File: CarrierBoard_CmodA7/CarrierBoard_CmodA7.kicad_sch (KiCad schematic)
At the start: 48 parts

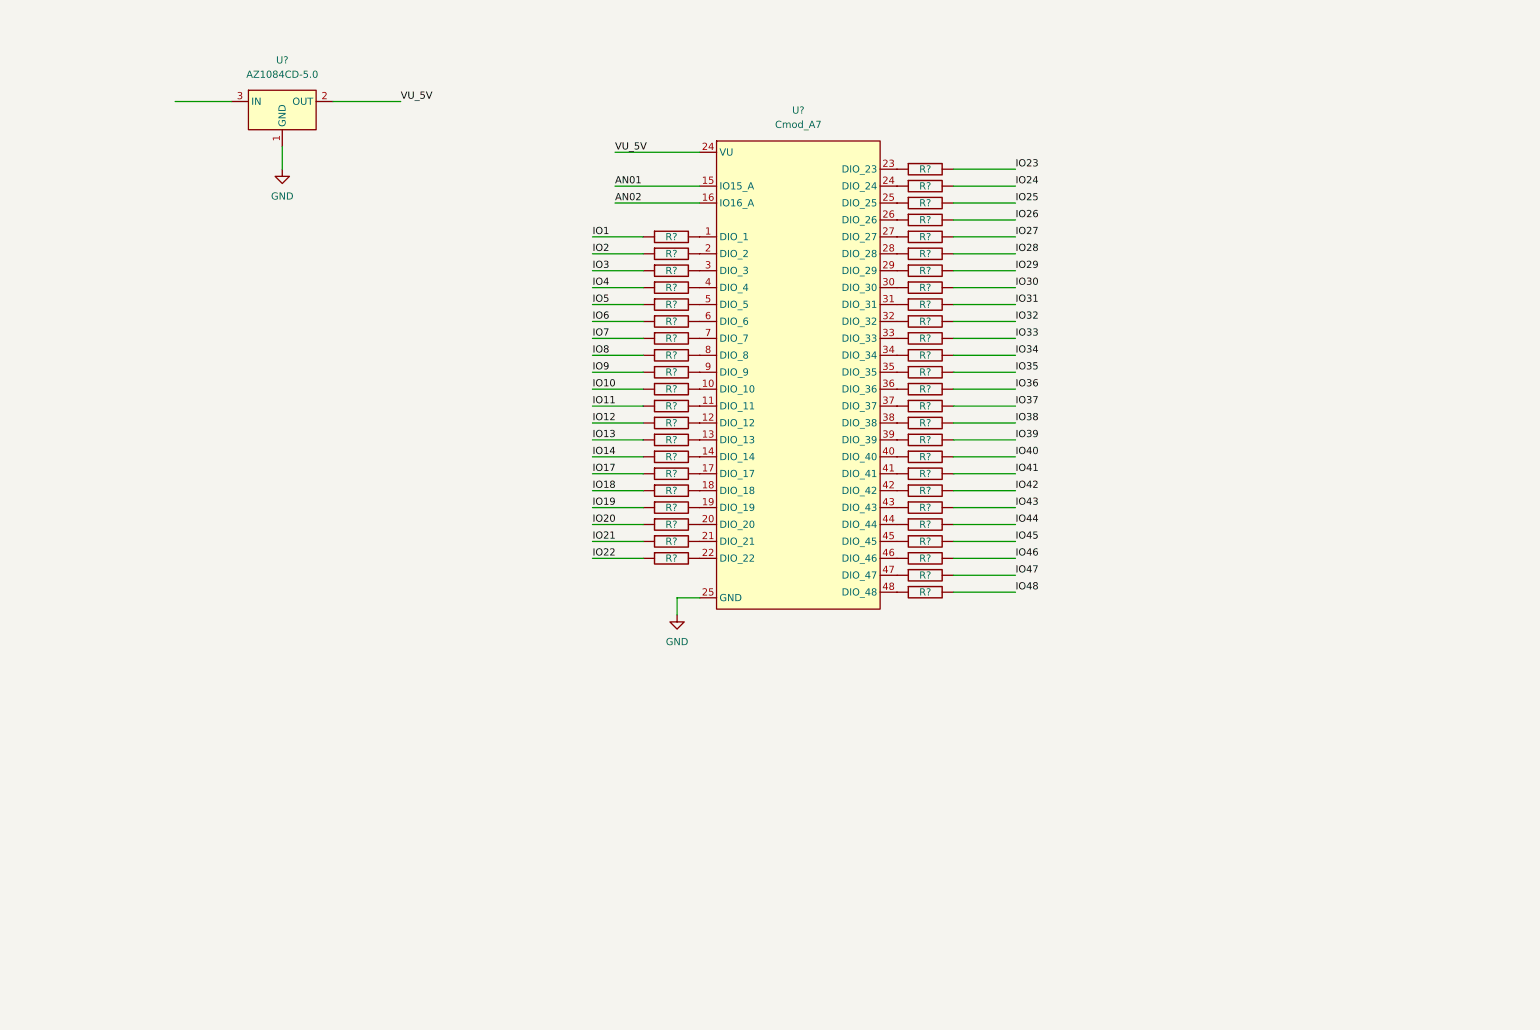
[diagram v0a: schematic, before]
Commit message: Añadidos conectores PMOD
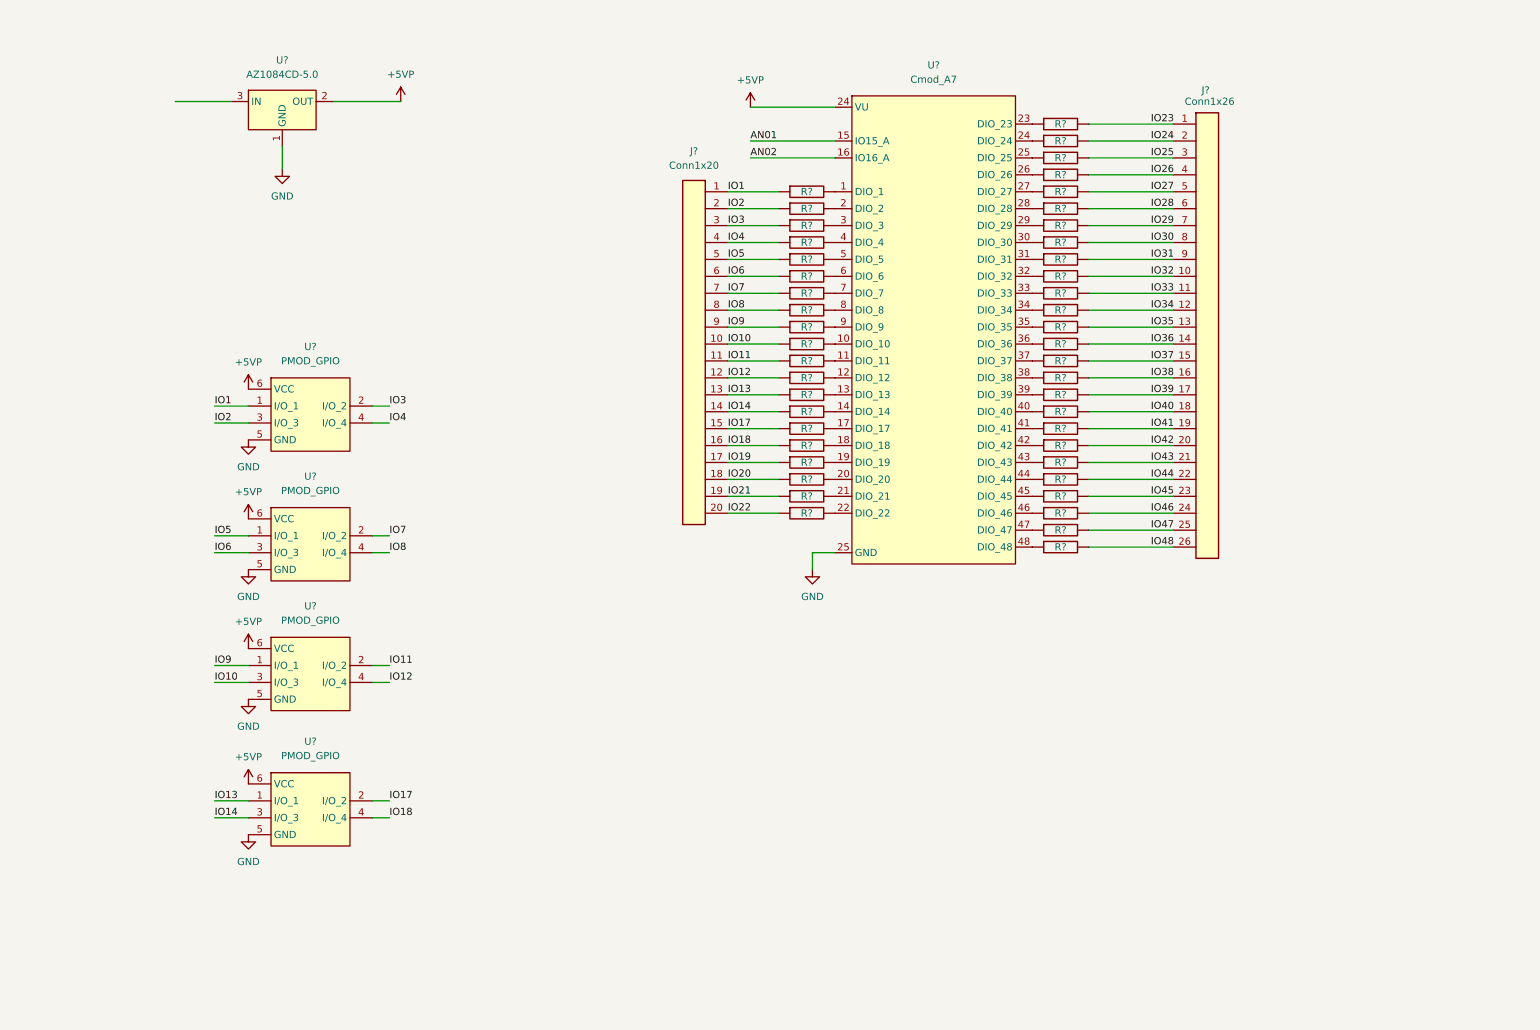
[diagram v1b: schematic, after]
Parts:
- added J?: Conn1x20, Connector_PinHeader_2.54mm:PinHeader_1x20_P2.54mm_Vertical, symbol Herranz - Gen Connectors:Conn1x20
- added J?: Conn1x26, Connector_PinHeader_2.54mm:PinHeader_1x26_P2.54mm_Vertical, symbol Herranz - Gen Connectors:Conn1x26
- added U? (x4): PMOD_GPIO, Connector_PinHeader_2.54mm:PinHeader_2x03_P2.54mm_Horizontal, symbol Herranz - Various:PMOD_GPIO
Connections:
- net GND: now also U?.5 (GND), U?.5 (GND), U?.5 (GND), U?.5 (GND)
- net IO1: now also J?.1 (Pin_1), U?.1 (I/O_1)
- net IO10: now also J?.10 (Pin_10), U?.3 (I/O_3)
- net IO11: now also J?.11 (Pin_11), U?.2 (I/O_2)
- net IO12: now also J?.12 (Pin_12), U?.4 (I/O_4)
- net IO13: now also J?.13 (Pin_13), U?.1 (I/O_1)
- net IO14: now also J?.14 (Pin_14), U?.3 (I/O_3)
- net IO17: now also J?.15 (Pin_15), U?.2 (I/O_2)
- net IO18: now also J?.16 (Pin_16), U?.4 (I/O_4)
- net IO19: now also J?.17 (Pin_17)
- net IO2: now also J?.2 (Pin_2), U?.3 (I/O_3)
- net IO20: now also J?.18 (Pin_18)
- net IO21: now also J?.19 (Pin_19)
- net IO22: now also J?.20 (Pin_20)
- net IO23: now also J?.1 (Pin_1)
- net IO24: now also J?.2 (Pin_2)
- net IO25: now also J?.3 (Pin_3)
- net IO26: now also J?.4 (Pin_4)
- net IO27: now also J?.5 (Pin_5)
- net IO28: now also J?.6 (Pin_6)
- net IO29: now also J?.7 (Pin_7)
- net IO3: now also J?.3 (Pin_3), U?.2 (I/O_2)
- net IO30: now also J?.8 (Pin_8)
- net IO31: now also J?.9 (Pin_9)
- net IO32: now also J?.10 (Pin_10)
- net IO33: now also J?.11 (Pin_11)
- net IO34: now also J?.12 (Pin_12)
- net IO35: now also J?.13 (Pin_13)
- net IO36: now also J?.14 (Pin_14)
- net IO37: now also J?.15 (Pin_15)
- net IO38: now also J?.16 (Pin_16)
- net IO39: now also J?.17 (Pin_17)
- net IO4: now also J?.4 (Pin_4), U?.4 (I/O_4)
- net IO40: now also J?.18 (Pin_18)
- net IO41: now also J?.19 (Pin_19)
- net IO42: now also J?.20 (Pin_20)
- net IO43: now also J?.21 (Pin_21)
- net IO44: now also J?.22 (Pin_22)
- net IO45: now also J?.23 (Pin_23)
- net IO46: now also J?.24 (Pin_24)
- net IO47: now also J?.25 (Pin_25)
- net IO48: now also J?.26 (Pin_26)
- net IO5: now also J?.5 (Pin_5), U?.1 (I/O_1)
- net IO6: now also J?.6 (Pin_6), U?.3 (I/O_3)
- net IO7: now also J?.7 (Pin_7), U?.2 (I/O_2)
- net IO8: now also J?.8 (Pin_8), U?.4 (I/O_4)
- net IO9: now also J?.9 (Pin_9), U?.1 (I/O_1)
- net VU_5V renamed +5VP
- net +5VP: now also U?.6 (VCC), U?.6 (VCC), U?.6 (VCC), U?.6 (VCC)
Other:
- moved on the sheet: R?, U?

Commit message: añadido red ADC
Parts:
- added R?: 140_P, Resistor_SMD:R_0603_1608Metric, symbol Herranz - Resistors (0603):140_P
- added R?: 845_P, Resistor_SMD:R_0603_1608Metric, symbol Herranz - Resistors (0603):845_P
- added R?: 1.0K_P, Resistor_SMD:R_0603_1608Metric, symbol Herranz - Resistors (0603):1.0K_P
- added R?: 2.32K_P, Resistor_SMD:R_0603_1608Metric, symbol Herranz - Resistors (0603):2.32K_P
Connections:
- net GND: now also R?.1, R?.2
- new net: R?.1, R?.2, R?.2
- new net GNDA: R?.1
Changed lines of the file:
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@@
 (kicad_sch (version 20211123) (generator eeschema)
   (paper "A4")
+  (junction (at 161 136) (diameter 0) (color 0 0 0 0)
+  )
+  (junction (at 134 151) (diameter 0) (color 0 0 0 0)
+  )
+  (junction (at 161 151) (diameter 0) (color 0 0 0 0)
+  )
   (wire (pts (xy 141 35) (xy 156 35))
     (stroke (width 0) (type default) (color 0 0 0 0))
@@
     (stroke (width 0) (type default) (color 0 0 0 0))
   )
+  (wire (pts (xy 152 136) (xy 161 136))
+    (stroke (width 0) (type default) (color 0 0 0 0))
+  )
   (wire (pts (xy 201 38) (xy 216 38))
     (stroke (width 0) (type default) (color 0 0 0 0))
@@
     (stroke (width 0) (type default) (color 0 0 0 0))
   )
+  (wire (pts (xy 128 136) (xy 142 136))
+    (stroke (width 0) (type default) (color 0 0 0 0))
+  )
   (wire (pts (xy 201 101) (xy 216 101))
     (stroke (width 0) (type default) (color 0 0 0 0))
   )
+  (wire (pts (xy 161 136) (xy 161 134))
+    (stroke (width 0) (type default) (color 0 0 0 0))
+  )
   (wire (pts (xy 201 95) (xy 216 95))
     (stroke (width 0) (type default) (color 0 0 0 0))
@@
     (stroke (width 0) (type default) (color 0 0 0 0))
   )
+  (wire (pts (xy 134 151) (xy 134 154))
+    (stroke (width 0) (type default) (color 0 0 0 0))
+  )
   (wire (pts (xy 46 134) (xy 52 134))
     (stroke (width 0) (type default) (color 0 0 0 0))
@@
     (stroke (width 0) (type default) (color 0 0 0 0))
   )
+  (wire (pts (xy 152 151) (xy 161 151))
+    (stroke (width 0) (type default) (color 0 0 0 0))
+  )
   (wire (pts (xy 74 88) (xy 77 88))
     (stroke (width 0) (type default) (color 0 0 0 0))
@@
     (stroke (width 0) (type default) (color 0 0 0 0))
   )
+  (wire (pts (xy 161 136) (xy 161 138))
+    (stroke (width 0) (type default) (color 0 0 0 0))
+  )
   (wire (pts (xy 137 107) (xy 146 107))
     (stroke (width 0) (type default) (color 0 0 0 0))
   )
+  (wire (pts (xy 161 154) (xy 161 151))
+    (stroke (width 0) (type default) (color 0 0 0 0))
+  )
   (wire (pts (xy 201 92) (xy 216 92))
     (stroke (width 0) (type default) (color 0 0 0 0))
@@
     (stroke (width 0) (type default) (color 0 0 0 0))
   )
+  (wire (pts (xy 128 151) (xy 134 151))
+    (stroke (width 0) (type default) (color 0 0 0 0))
+  )
   (wire (pts (xy 137 104) (xy 146 104))
     (stroke (width 0) (type default) (color 0 0 0 0))
@@
     (stroke (width 0) (type default) (color 0 0 0 0))
   )
+  (wire (pts (xy 134 151) (xy 142 151))
+    (stroke (width 0) (type default) (color 0 0 0 0))
+  )
   (wire (pts (xy 137 74) (xy 146 74))
     (stroke (width 0) (type default) (color 0 0 0 0))
@@
   )
   (wire (pts (xy 201 65) (xy 216 65))
+    (stroke (width 0) (type default) (color 0 0 0 0))
+  )
+  (wire (pts (xy 161 151) (xy 161 148))
     (stroke (width 0) (type default) (color 0 0 0 0))
   )
@@
     )
     (pin "1")
+  )
+  (symbol (lib_id "Herranz - Resistors (0603):140_P") (at 147 135 0) (unit 1)
+    (in_bom yes) (on_board yes) (fields_autoplaced)
+    (property "Reference" "R?" (id 0) (at 147 127 0))
+    (property "Value" "140_P" (id 1) (at 147 129.54 0))
+    (property "Footprint" "Resistor_SMD:R_0603_1608Metric" (id 2) (at 147 132 0)
+      (effects (font (size 1.27 1.27)) hide)
+    )
+    (property "Datasheet" "" (id 3) (at 147 135 0)
+      (effects (font (size 1.27 1.27)) hide)
+    )
+    (property "Size" "0603" (id 4) (at 147 132.08 0))
+    (property "Precision" "X" (id 5) (at 147 135 0)
+      (effects (font (size 1.27 1.27)) hide)
+    )
+    (property "PartNum1" "RN73H1JTTD1400F50 " (id 6) (at 147 135 0)
+      (effects (font (size 1.27 1.27)) hide)
+    )
+    (property "Mnf1" "KOA Speer" (id 7) (at 147 135 0)
+      (effects (font (size 1.27 1.27)) hide)
+    )
+    (pin "1")
+    (pin "2")
   )
   (symbol (lib_id "Herranz - Resistors (0603):1.0K") (at 196 49 0) (unit 1)
@@
     (pin "2")
   )
+  (symbol (lib_id "Herranz - Resistors (0603):845_P") (at 147 150 0) (unit 1)
+    (in_bom yes) (on_board yes) (fields_autoplaced)
+    (property "Reference" "R?" (id 0) (at 147 142.43 0))
+    (property "Value" "845_P" (id 1) (at 147 144.97 0))
+    (property "Footprint" "Resistor_SMD:R_0603_1608Metric" (id 2) (at 147 147 0)
+      (effects (font (size 1.27 1.27)) hide)
+    )
+    (property "Datasheet" "" (id 3) (at 147 150 0)
+      (effects (font (size 1.27 1.27)) hide)
+    )
+    (property "Size" "0603" (id 4) (at 147 147.51 0))
+    (pin "1")
+    (pin "2")
+  )
   (symbol (lib_id "Herranz - Resistors (0603):1.0K") (at 196 94 0) (unit 1)
     (in_bom yes) (on_board yes)
@@
     (pin "2")
   )
+  (symbol (lib_id "power:GNDA") (at 134 154 0) (unit 1)
+    (in_bom yes) (on_board yes) (fields_autoplaced)
+    (property "Reference" "#PWR?" (id 0) (at 134 160.35 0)
+      (effects (font (size 1.27 1.27)) hide)
+    )
+    (property "Value" "GNDA" (id 1) (at 134 159.21 0))
+    (property "Footprint" "" (id 2) (at 134 154 0)
+      (effects (font (size 1.27 1.27)) hide)
+    )
+    (property "Datasheet" "" (id 3) (at 134 154 0)
+      (effects (font (size 1.27 1.27)) hide)
+    )
+    (pin "1")
+  )
   (symbol (lib_id "Herranz - Resistors (0603):1.0K") (at 196 109 0) (unit 1)
     (in_bom yes) (on_board yes)
@@
     (pin "2")
   )
+  (symbol (lib_id "power:GND") (at 161 154 0) (unit 1)
+    (in_bom yes) (on_board yes) (fields_autoplaced)
+    (property "Reference" "#PWR?" (id 0) (at 161 160.35 0)
+      (effects (font (size 1.27 1.27)) hide)
+    )
+    (property "Value" "GND" (id 1) (at 161 158.8 0))
+    (property "Footprint" "" (id 2) (at 161 154 0)
+      (effects (font (size 1.27 1.27)) hide)
+    )
+    (property "Datasheet" "" (id 3) (at 161 154 0)
+      (effects (font (size 1.27 1.27)) hide)
+    )
+    (pin "1")
+  )
   (symbol (lib_id "Herranz - Resistors (0603):1.0K") (at 196 67 0) (unit 1)
     (in_bom yes) (on_board yes)
@@
     (property "Size" "0603" (id 4) (at 196 55.61 0)
       (effects (font (size 1.27 1.27)) hide)
+    )
+    (pin "1")
+    (pin "2")
+  )
+  (symbol (lib_id "Herranz - Resistors (0603):1.0K_P") (at 160 143 90) (unit 1)
+    (in_bom yes) (on_board yes) (fields_autoplaced)
+    (property "Reference" "R?" (id 0) (at 163.83 140.4599 90)
+      (effects (font (size 1.27 1.27)) (justify right))
+    )
+    (property "Value" "1.0K_P" (id 1) (at 163.83 142.9999 90)
+      (effects (font (size 1.27 1.27)) (justify right))
+    )
+    (property "Footprint" "Resistor_SMD:R_0603_1608Metric" (id 2) (at 157 143 0)
+      (effects (font (size 1.27 1.27)) hide)
+    )
+    (property "Datasheet" "" (id 3) (at 160 143 0)
+      (effects (font (size 1.27 1.27)) hide)
+    )
+    (property "Size" "0603" (id 4) (at 163.83 145.5399 90)
+      (effects (font (size 1.27 1.27)) (justify right))
     )
     (pin "1")
@@
     (pin "2")
   )
+  (symbol (lib_id "Herranz - Resistors (0603):2.32K_P") (at 160 129 90) (unit 1)
+    (in_bom yes) (on_board yes) (fields_autoplaced)
+    (property "Reference" "R?" (id 0) (at 163.83 126.4599 90)
+      (effects (font (size 1.27 1.27)) (justify right))
+    )
+    (property "Value" "2.32K_P" (id 1) (at 163.83 128.9999 90)
+      (effects (font (size 1.27 1.27)) (justify right))
+    )
+    (property "Footprint" "Resistor_SMD:R_0603_1608Metric" (id 2) (at 157 129 0)
+      (effects (font (size 1.27 1.27)) hide)
+    )
+    (property "Datasheet" "" (id 3) (at 160 129 0)
+      (effects (font (size 1.27 1.27)) hide)
+    )
+    (property "Size" "0603" (id 4) (at 163.83 131.5399 90)
+      (effects (font (size 1.27 1.27)) (justify right))
+    )
+    (pin "1")
+    (pin "2")
+  )
   (symbol (lib_id "Herranz - Resistors (0603):1.0K") (at 196 85 0) (unit 1)
     (in_bom yes) (on_board yes)
@@
       (reference "#PWR?") (unit 1) (value "GND") (footprint "")
     )
+    (path "/bcaf2dca-bfb6-45b7-bff9-b0d7d064715a"
+      (reference "#PWR?") (unit 1) (value "GNDA") (footprint "")
+    )
+    (path "/beb53e2f-63cb-4982-a0e9-8eccccd29909"
+      (reference "#PWR?") (unit 1) (value "GND") (footprint "")
+    )
     (path "/e23fe0f2-2b10-4e4e-a248-1590767a0e0e"
       (reference "#PWR?") (unit 1) (value "GND") (footprint "")
@@
       (reference "R?") (unit 1) (value "1.0K") (footprint "Resistor_SMD:R_0603_1608Metric")
     )
+    (path "/4b68fabc-0578-4223-a045-7ebbc31dc0d9"
+      (reference "R?") (unit 1) (value "140_P") (footprint "Resistor_SMD:R_0603_1608Metric")
+    )
     (path "/4c0f8c6c-ed32-407d-8144-2572e6613b1a"
       (reference "R?") (unit 1) (value "1.0K") (footprint "Resistor_SMD:R_0603_1608Metric")
@@
       (reference "R?") (unit 1) (value "1.0K") (footprint "Resistor_SMD:R_0603_1608Metric")
     )
+    (path "/62dc1d02-190f-4c9d-8ded-2c7f4b299c50"
+      (reference "R?") (unit 1) (value "845_P") (footprint "Resistor_SMD:R_0603_1608Metric")
+    )
     (path "/682ef0b5-4757-486e-bfa0-dbc2cfb3c97d"
       (reference "R?") (unit 1) (value "1.0K") (footprint "Resistor_SMD:R_0603_1608Metric")
@@
       (reference "R?") (unit 1) (value "1.0K") (footprint "Resistor_SMD:R_0603_1608Metric")
     )
+    (path "/d7458376-c896-485f-8b16-199988aa6ff9"
+      (reference "R?") (unit 1) (value "1.0K_P") (footprint "Resistor_SMD:R_0603_1608Metric")
+    )
     (path "/e6af4738-fd82-4f32-a4b3-119fd5772832"
       (reference "R?") (unit 1) (value "1.0K") (footprint "Resistor_SMD:R_0603_1608Metric")
@@
       (reference "R?") (unit 1) (value "1.0K") (footprint "Resistor_SMD:R_0603_1608Metric")
     )
+    (path "/eecb6215-4617-42e3-ba7c-dfb8b02cb50b"
+      (reference "R?") (unit 1) (value "2.32K_P") (footprint "Resistor_SMD:R_0603_1608Metric")
+    )
     (path "/ef924c6c-191d-4eb3-9a1a-733d6c273e6e"

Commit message: esquema ordenado
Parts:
- added R?: 2.32K_P, Resistor_SMD:R_0603_1608Metric, symbol Herranz - Resistors (0603):2.32K_P
- added R?: 1.0K_P, Resistor_SMD:R_0603_1608Metric, symbol Herranz - Resistors (0603):1.0K_P
- added R?: 845_P, Resistor_SMD:R_0603_1608Metric, symbol Herranz - Resistors (0603):845_P
- added R?: 140_P, Resistor_SMD:R_0603_1608Metric, symbol Herranz - Resistors (0603):140_P
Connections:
- net GND: now also R?.1, R?.2
- net GNDA: now also R?.1
- new net: R?.1, R?.2, R?.2
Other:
- note added: "ADC adapters"
- note added: "PMOD x4"
- moved on the sheet: J?, R?, U?
